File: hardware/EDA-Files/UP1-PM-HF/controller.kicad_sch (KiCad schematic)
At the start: 25 parts, among them J101 UP1-Prog, U100 RP2040, U101 W25Q128JVS, Y100 12MHz

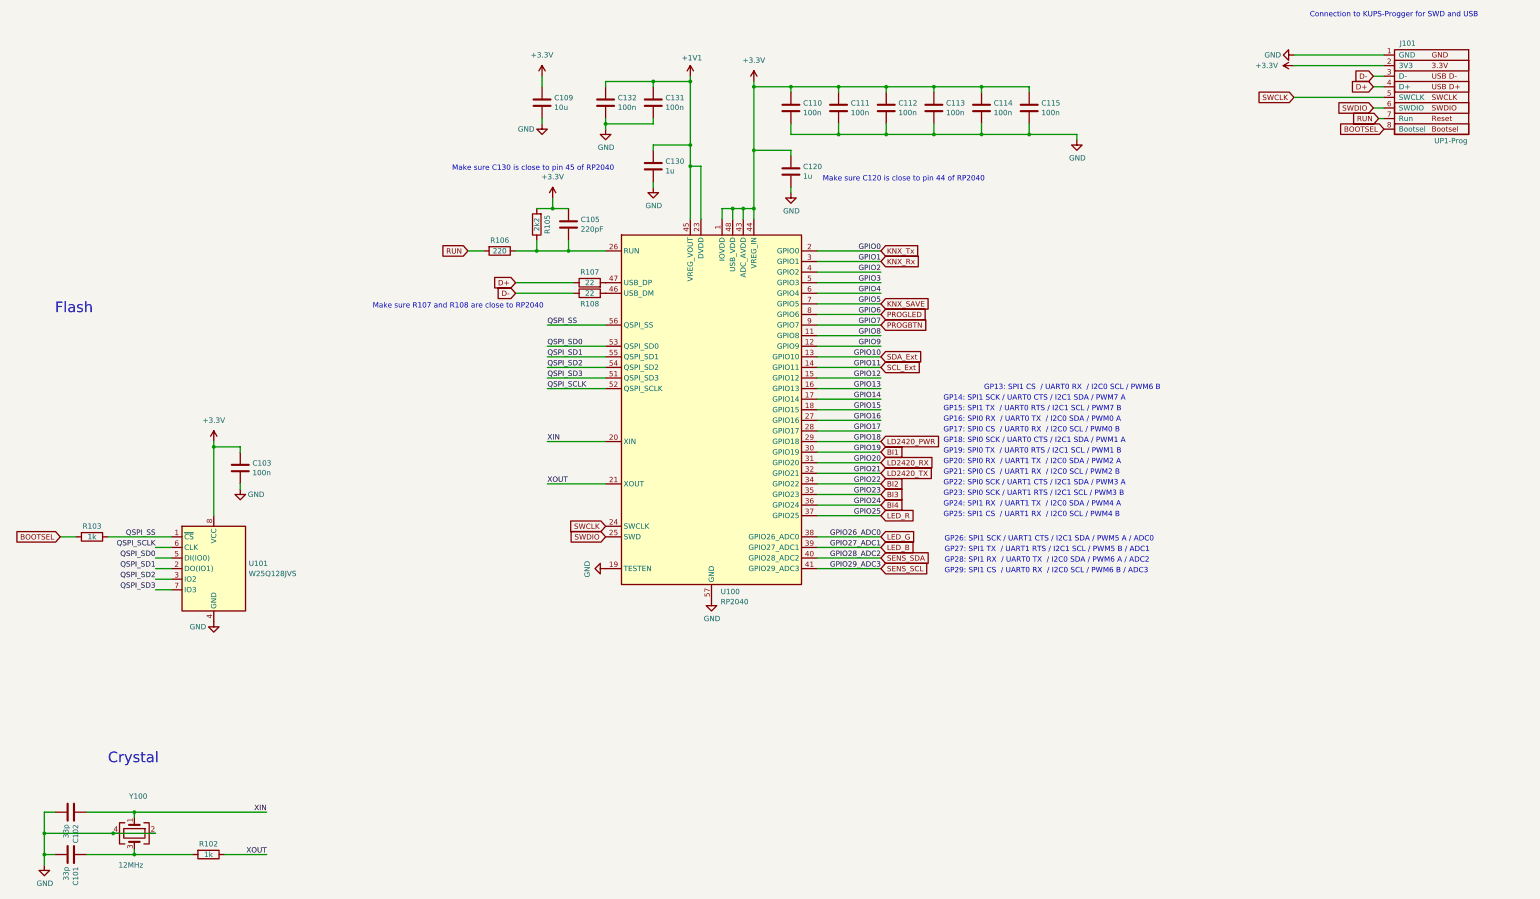
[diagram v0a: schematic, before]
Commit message: UP1-PM-HF V00.20: - add reset IC
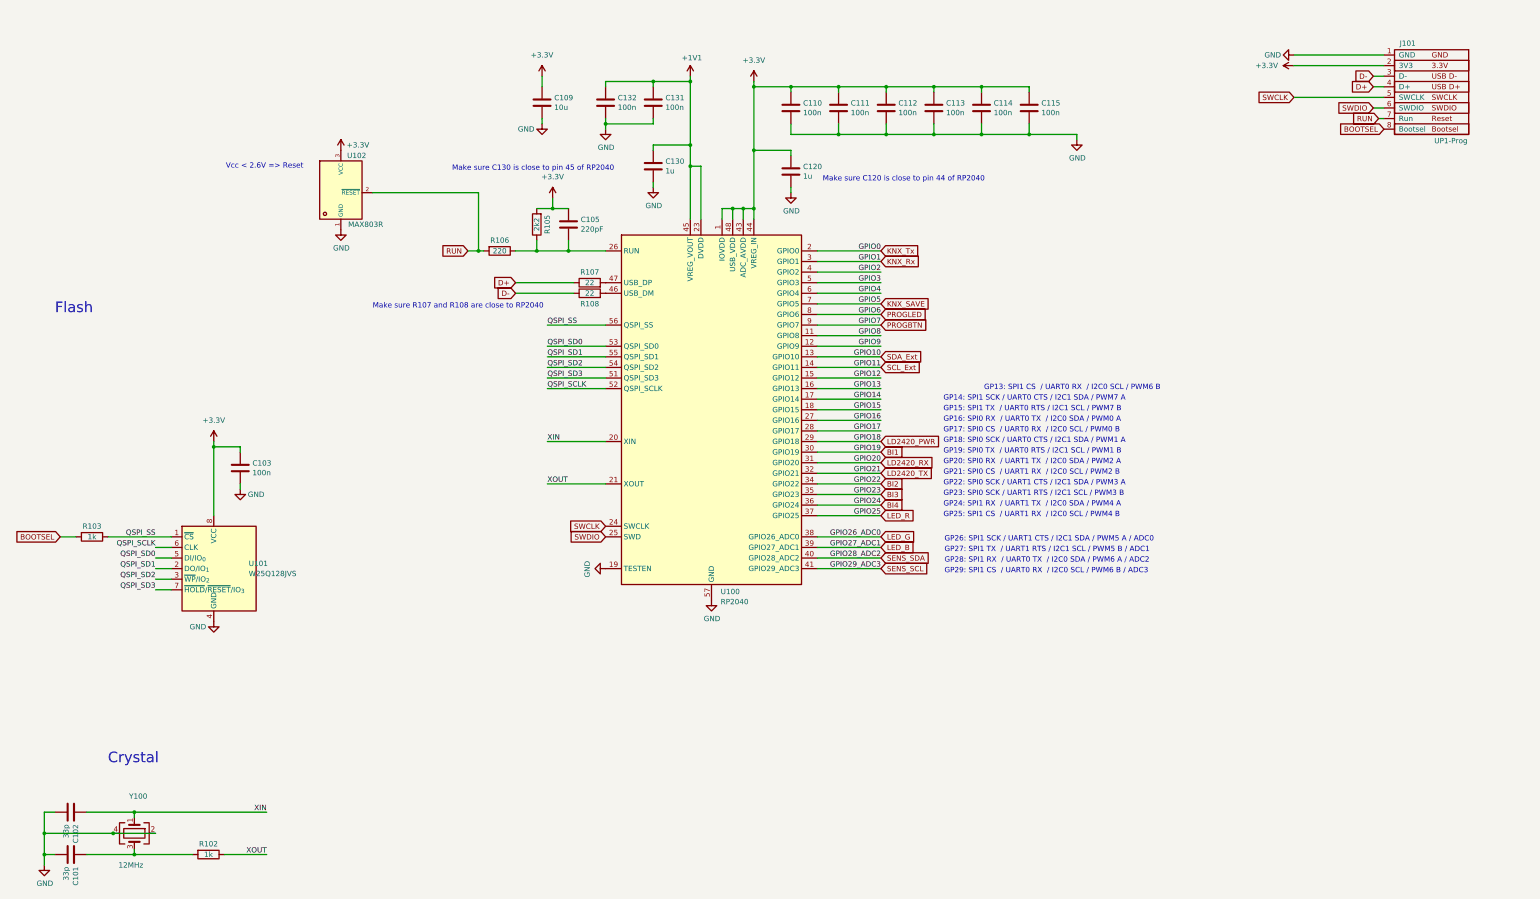
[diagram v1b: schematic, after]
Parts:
- added U102: MAX803R, Package_TO_SOT_SMD:SOT-23, symbol EasyEDALib:MAX809R
- U101: footprint Package_SO:SOIC-8_5.23x5.23mm_P1.27mm -> Package_SO:SOIC-8_5.3x5.3mm_P1.27mm
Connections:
- net +3.3V: now also U102.3 (VCC)
- net GND: now also U102.1 (GND)
- net RUN: now also U102.2 (~{RESET})
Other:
- note added: "Vcc < 2.6V => Reset"
- note removed: "Connection to KUPS-Progger for SWD and USB"
- moved on the sheet: U101

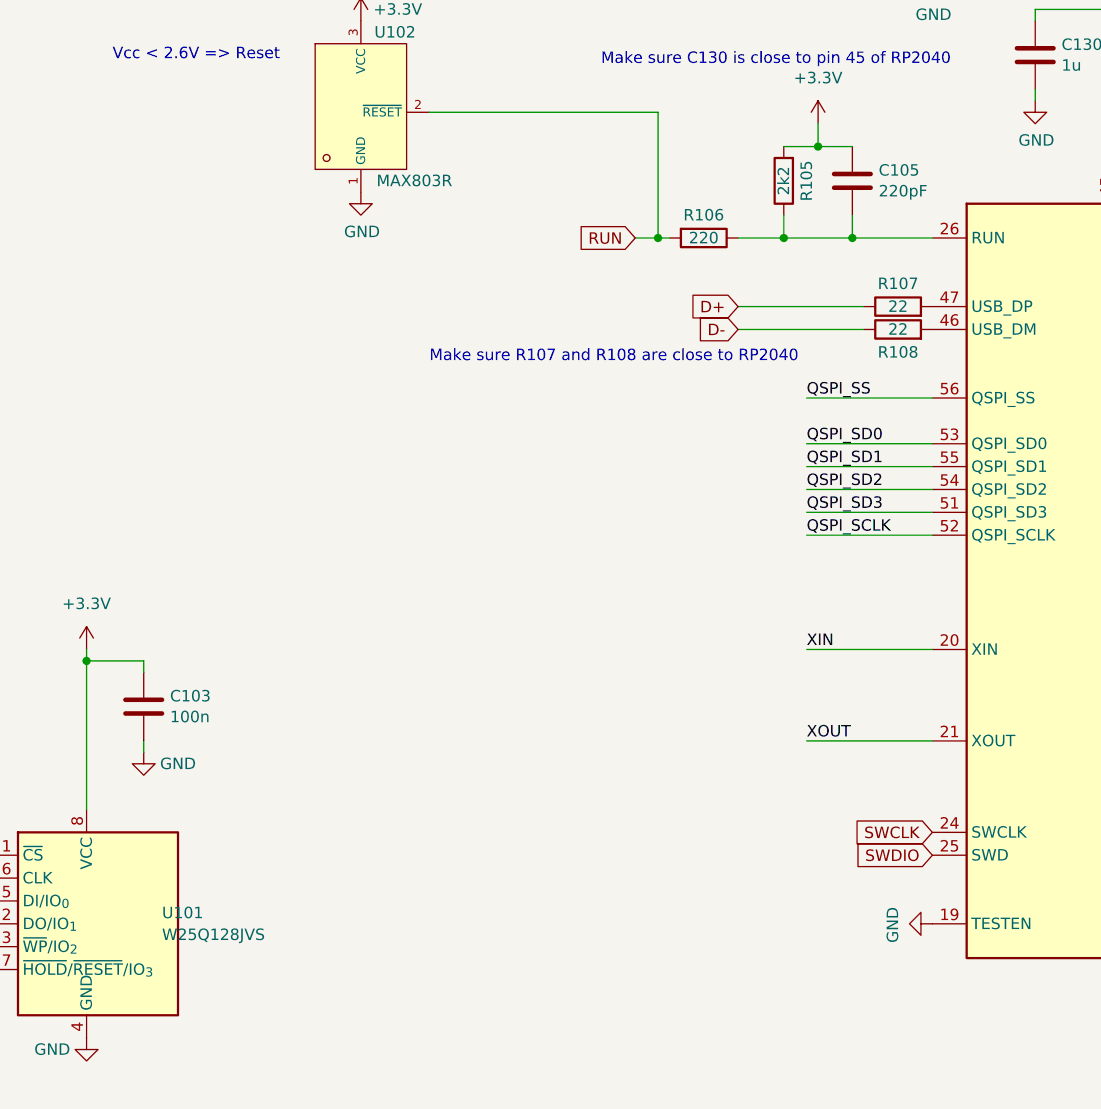
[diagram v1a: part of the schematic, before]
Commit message: UP1-PM-HF V00.21 * variable Flash (W25Q) * move FP to OpenKNX KiCAD Lib * increase Pad size for hand solder pins * change RP2040 reset circuit
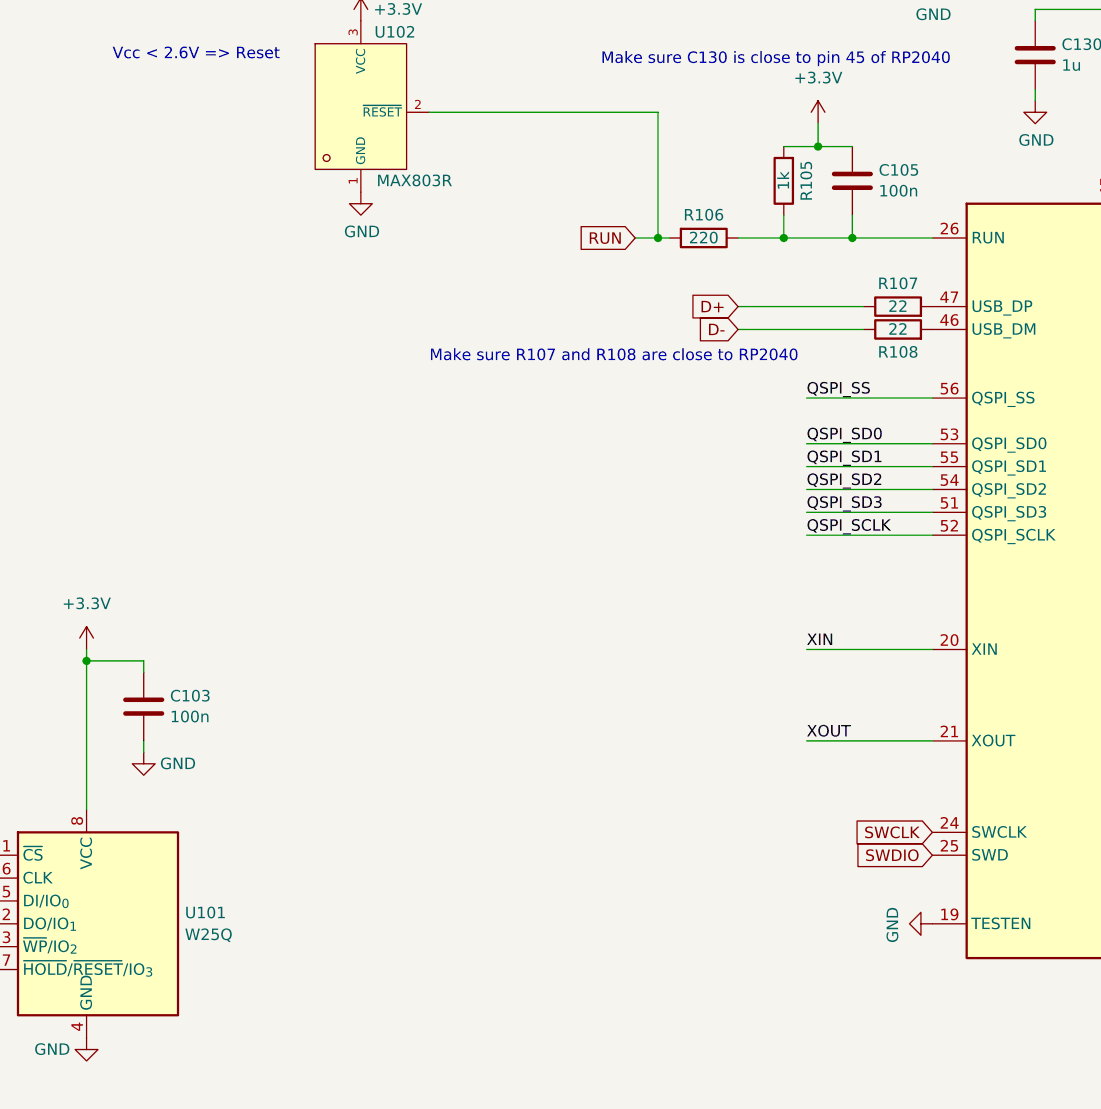
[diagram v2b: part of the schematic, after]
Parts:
- C105: value 220pF -> 100n
- R105: value 2k2 -> 1k
- U101: value W25Q128JVS -> W25Q
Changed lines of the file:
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@@
 	(title_block
 		(title "UP1-PM-HF")
-		(date "2025-12-09")
-		(rev "V00.20")
+		(date "2026-02-06")
+		(rev "V00.21")
 		(company "OpenKNX")
 		(comment 1 "by Ing-Dom <dom@ing-dom.de>")
@@
 			)
 		)
-		(property "Value" "220pF"
+		(property "Value" "100n"
 			(at 173.101 78.613 0)
 			(effects
@@
 			)
 		)
-		(property "Value" "2k2"
+		(property "Value" "1k"
 			(at 162.56 77.47 90)
 			(effects
@@
 			)
 		)
-		(property "Datasheet" "https://atta.szlcsc.com/upload/public/pdf/source/20210806/C891276_124AE56F58E44342B6D8BB3E7125FD65.pdf"
+		(property "Datasheet" ""
 			(at 91.44 82.55 0)
 			(effects
@@
 		(fields_autoplaced yes)
 		(property "Reference" "U101"
-			(at 93.472 158.8079 0)
+			(at 96.012 158.8078 0)
 			(effects
 				(font
@@
 			)
 		)
-		(property "Value" "W25Q128JVS"
-			(at 93.472 161.2321 0)
+		(property "Value" "W25Q"
+			(at 96.012 161.2321 0)
 			(effects
 				(font
